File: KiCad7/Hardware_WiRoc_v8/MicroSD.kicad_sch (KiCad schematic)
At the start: 13 parts, among them J3 Micro_SD_Card_Det1

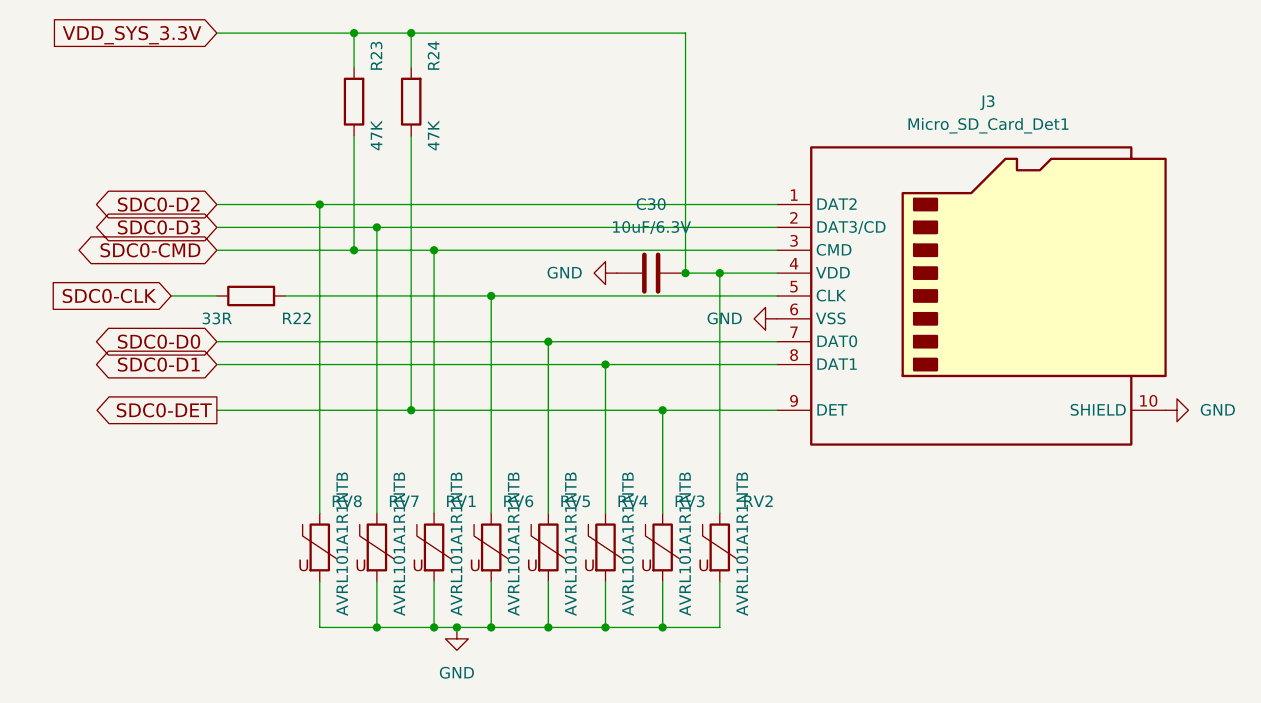
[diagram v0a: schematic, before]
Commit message: wiroc v8 layout work
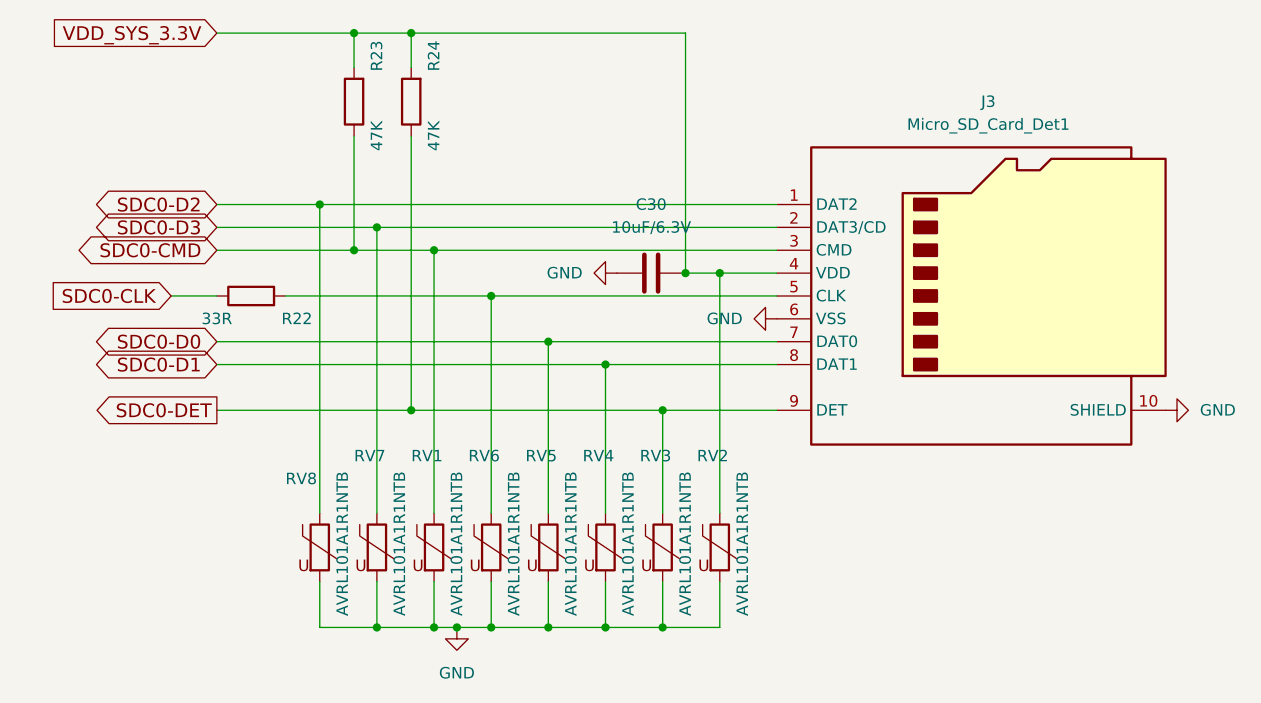
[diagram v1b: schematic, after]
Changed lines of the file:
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@@
   (symbol (lib_id "Device:Varistor") (at 119.38 99.06 0) (unit 1)
     (in_bom yes) (on_board yes) (dnp no)
-    (property "Reference" "RV2" (at 121.92 93.98 0)
+    (property "Reference" "RV2" (at 116.84 88.9 0)
       (effects (font (size 1.27 1.27)) (justify left))
     )
@@
   (symbol (lib_id "Device:Varistor") (at 106.68 99.06 0) (unit 1)
     (in_bom yes) (on_board yes) (dnp no)
-    (property "Reference" "RV4" (at 107.95 93.98 0)
+    (property "Reference" "RV4" (at 104.14 88.9 0)
       (effects (font (size 1.27 1.27)) (justify left))
     )
@@
   (symbol (lib_id "Device:Varistor") (at 113.03 99.06 0) (unit 1)
     (in_bom yes) (on_board yes) (dnp no)
-    (property "Reference" "RV3" (at 114.3 93.98 0)
+    (property "Reference" "RV3" (at 110.49 88.9 0)
       (effects (font (size 1.27 1.27)) (justify left))
     )
@@
   (symbol (lib_id "Device:Varistor") (at 93.98 99.06 0) (unit 1)
     (in_bom yes) (on_board yes) (dnp no)
-    (property "Reference" "RV6" (at 95.25 93.98 0)
+    (property "Reference" "RV6" (at 91.44 88.9 0)
       (effects (font (size 1.27 1.27)) (justify left))
     )
@@
   (symbol (lib_id "Device:Varistor") (at 87.63 99.06 0) (unit 1)
     (in_bom yes) (on_board yes) (dnp no)
-    (property "Reference" "RV1" (at 88.9 93.98 0)
+    (property "Reference" "RV1" (at 85.09 88.9 0)
       (effects (font (size 1.27 1.27)) (justify left))
     )
@@
   (symbol (lib_id "Device:Varistor") (at 74.93 99.06 0) (unit 1)
     (in_bom yes) (on_board yes) (dnp no)
-    (property "Reference" "RV8" (at 76.2 93.98 0)
+    (property "Reference" "RV8" (at 71.12 91.44 0)
       (effects (font (size 1.27 1.27)) (justify left))
     )
@@
   (symbol (lib_id "Device:Varistor") (at 100.33 99.06 0) (unit 1)
     (in_bom yes) (on_board yes) (dnp no)
-    (property "Reference" "RV5" (at 101.6 93.98 0)
+    (property "Reference" "RV5" (at 97.79 88.9 0)
       (effects (font (size 1.27 1.27)) (justify left))
     )
@@
   (symbol (lib_id "Device:Varistor") (at 81.28 99.06 0) (unit 1)
     (in_bom yes) (on_board yes) (dnp no)
-    (property "Reference" "RV7" (at 82.55 93.98 0)
-      (effects (font (size 1.27 1.27)) (justify left))
-    )
+    (property "Reference" "RV7" (at 78.74 88.9 0)
+      (effects (font (size 1.27 1.27)) (justify left))
+    )
